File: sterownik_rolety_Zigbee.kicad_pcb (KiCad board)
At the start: 2 copper layers, 39 parts, among them J1 282836-5, J2 1725669, J3 53398-0567, Q1 BT136-600, Q2 BT136-600, Q3 MOC3032M, Q4 MOC3032M, U1 LTV-817, U2 LTV-817, U3 IRM-01-3.3, Y1 TXC 7R-32.000MEEV-T

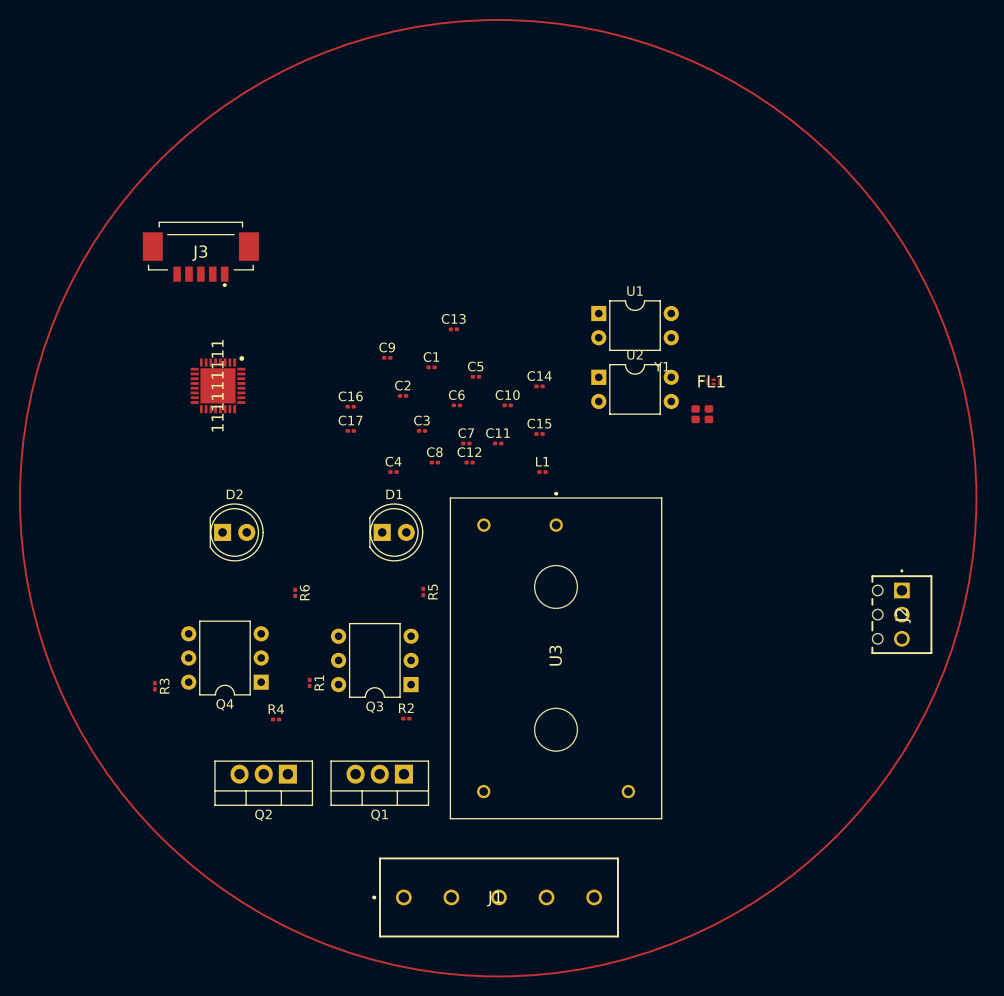
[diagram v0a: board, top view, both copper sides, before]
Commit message: kryształ kondensatory i interfejs podłączone z mikrokontrolerem
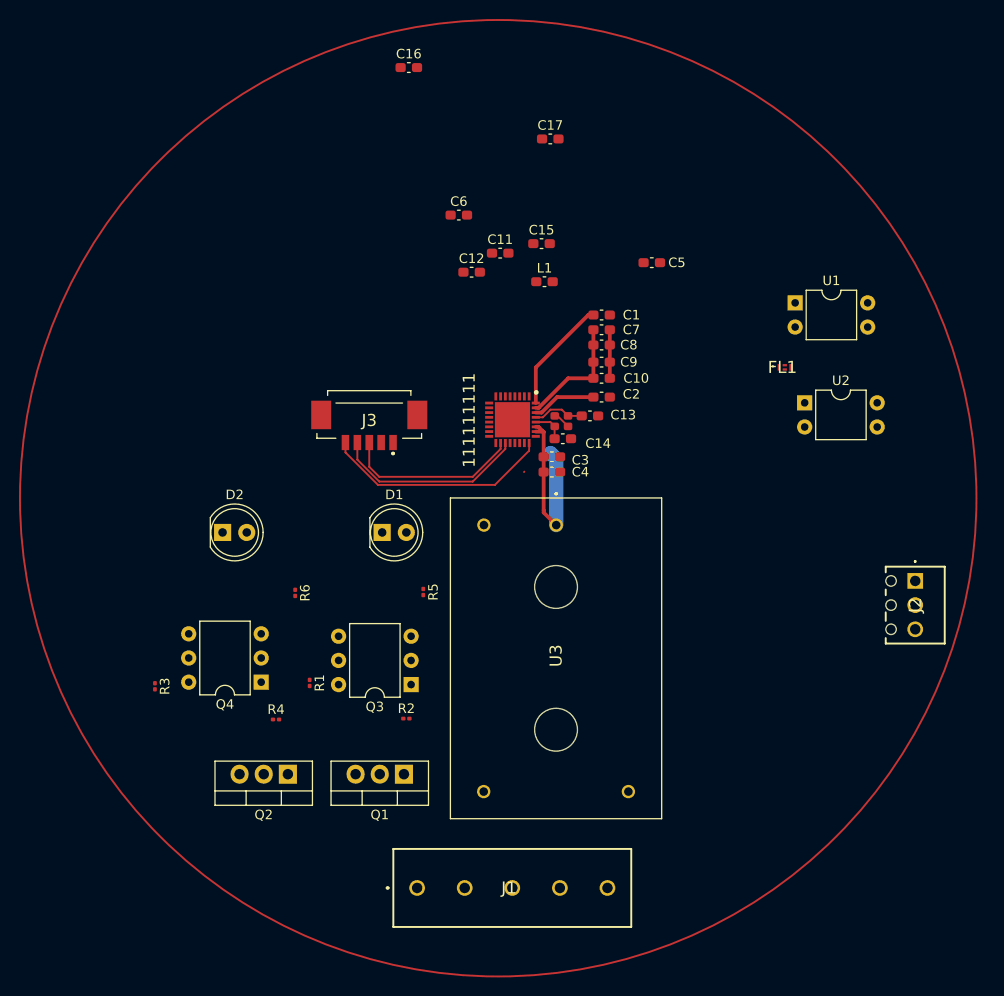
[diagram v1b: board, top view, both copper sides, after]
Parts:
- C1, C10, C11, C12, C13, C14, C15, C16, C17, C2, C3, C4, C5, C6, C7, C8, C9: footprint Capacitor_SMD:C_0201_0603Metric -> Capacitor_SMD:C_0603_1608Metric_Pad1.08x0.95mm_HandSolder
- L1: footprint Inductor_SMD:L_0201_0603Metric -> Capacitor_SMD:C_0603_1608Metric_Pad1.08x0.95mm_HandSolder
- moved C17 37.2 mm to (132.5, 60.0)
- moved C16 36.2 mm to (117.6, 52.5)
- moved 111111111 31.1 mm to (128.5, 89.5)
- moved J3 25.0 mm to (113.5, 89.6)
- moved C9 22.5 mm to (137.9, 83.5)
- moved C5 22.0 mm to (143.1, 73.0)
- moved U2 21.8 mm to (159.2, 87.7)
- moved C8 21.4 mm to (137.9, 81.7)
- moved C2 20.9 mm to (137.9, 87.1)
- moved U1 20.7 mm to (158.2, 77.2)
- moved C11 20.0 mm to (127.2, 72.0)
- moved C12 20.0 mm to (124.2, 74.0)
- moved C15 20.0 mm to (131.6, 71.0)
- moved C6 20.0 mm to (122.9, 68.0)
- moved L1 20.0 mm to (131.9, 75.0)
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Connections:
- C13 pad 1: GND -> Net-(111111111-OSC_IN)
- C13 pad 2: Net-(111111111-OSC_IN) -> GND
- C14 pad 1: GND -> Net-(111111111-OSC_OUT)
- C14 pad 2: Net-(111111111-OSC_OUT) -> GND
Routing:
- net VDD: track 0.00 -> 51.5 mm
- net Negated Reset: track 0.00 -> 24.0 mm
- net JTMS/SWDIO: track 0.00 -> 20.3 mm
- net JTCK/SWCLK: track 0.00 -> 18.6 mm
- net GND: track 0.00 -> 6.96 mm
- net Net-(111111111-OSC_IN): track 0.00 -> 5.43 mm
- net Net-(111111111-OSC_OUT): track 0.00 -> 3.48 mm

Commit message: połączenie ścieżkami, wylanie masy
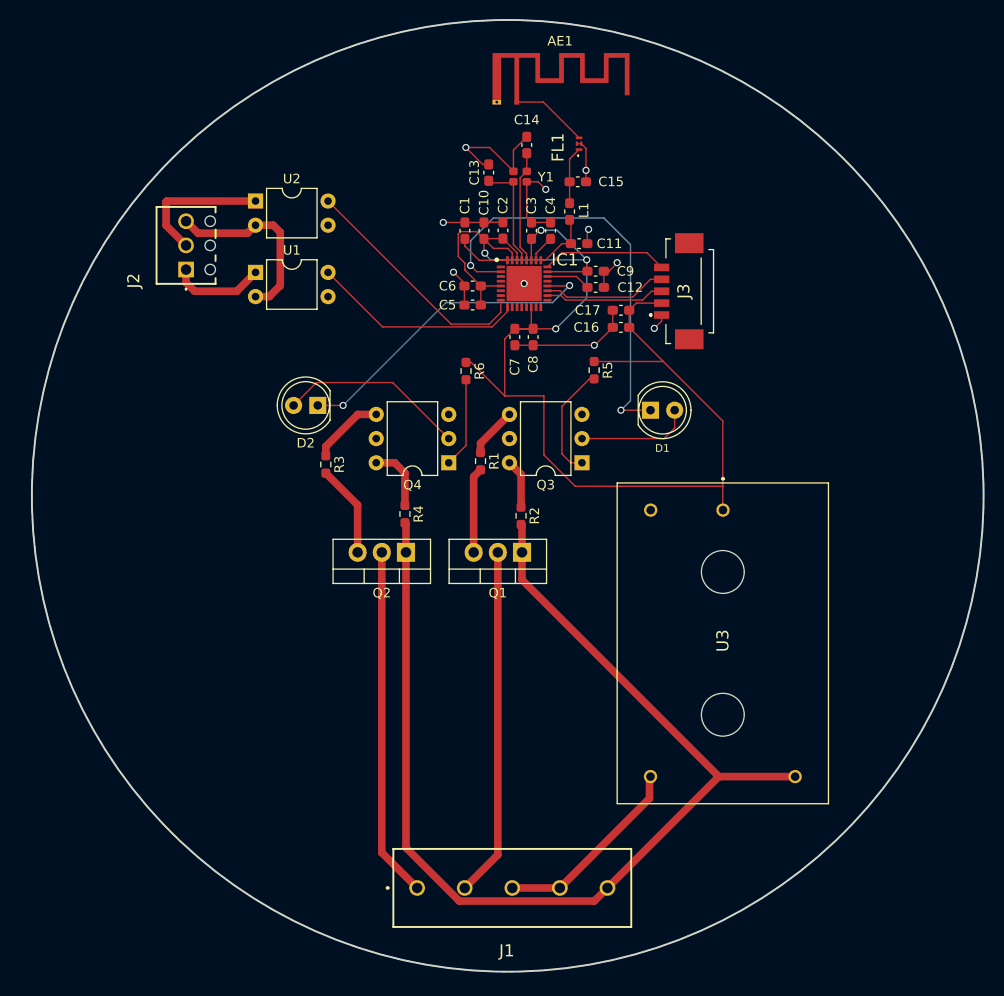
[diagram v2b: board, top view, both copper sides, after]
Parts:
- added AE1: Antenna, RF_Antenna:Texas_SWRA117D_2.4GHz_Right, F.Cu at (128.9, 56.1)
- L1: footprint Capacitor_SMD:C_0603_1608Metric_Pad1.08x0.95mm_HandSolder -> Inductor_SMD:L_0603_1608Metric_Pad1.05x0.95mm_HandSolder
- R1, R2, R3, R4, R5, R6: footprint Resistor_SMD:R_0201_0603Metric -> Resistor_SMD:R_0603_1608Metric_Pad0.98x0.95mm_HandSolder
- moved J2 83.3 mm to (94.2, 73.7), turned to 90 degrees
- moved U2 61.5 mm to (101.5, 66.5)
- moved U1 56.8 mm to (101.5, 74.0)
- moved J3 35.7 mm to (146.5, 76.0), turned to -90 degrees
- moved C16 35.2 mm to (139.9, 79.8), turned to 180 degrees
- moved FL1 31.9 mm to (135.5, 60.5), turned to 90 degrees
- moved C14 31.1 mm to (130.0, 60.6), turned to -90 degrees
- moved D1 31.0 mm to (143.0, 88.5)
- moved Q4 30.3 mm to (121.8, 94.0)
- moved R5 29.4 mm to (137.1, 84.3)
- moved Q3 29.4 mm to (135.8, 94.0)
- moved R1 29.4 mm to (125.1, 93.9)
- moved R3 29.4 mm to (108.9, 94.2)
- moved R6 29.4 mm to (123.6, 84.4)
- moved C13 27.7 mm to (126.0, 63.5), turned to -90 degrees
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- renumbered 111111111 to IC1
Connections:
- C1 pad 1: VDD -> Net-(IC1-VCAP)
- C13 pad 1: Net-(111111111-OSC_IN) -> GND
- C13 pad 2: GND -> Net-(IC1-OSC_IN)
- C14 pad 1: Net-(111111111-OSC_OUT) -> GND
- C14 pad 2: GND -> Net-(IC1-OSC_OUT)
- C4 pad 1: VDD -> Net-(IC1-VDDHPA)
- IC1 pad 26: VDD -> Net-(IC1-VDDHPA)
- IC1 pad 28: Net-(111111111-OSC_OUT) -> Net-(IC1-OSC_OUT)
- IC1 pad 29: Net-(111111111-OSC_IN) -> Net-(IC1-OSC_IN)
- IC1 pad 32: VDD -> Net-(IC1-VCAP)
- Y1 pad 1: Net-(111111111-OSC_OUT) -> Net-(IC1-OSC_OUT)
- Y1 pad 3: Net-(111111111-OSC_IN) -> Net-(IC1-OSC_IN)
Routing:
- net L_connector: track 0.00 -> 117.9 mm
- net VDD: track 51.5 -> 148.3 mm, vias 0 -> 4
- net GND: track 6.96 -> 56.7 mm, vias 0 -> 10
- net Motor_output_1: track 0.00 -> 45.9 mm, vias 0 -> 2
- net Q2_connector: track 0.00 -> 36.8 mm
- net Q1_connector: track 0.00 -> 36.7 mm
- net Motor_output_2: track 0.00 -> 34.0 mm, vias 0 -> 2
- net Net-(IC1-PA1): track 0.00 -> 25.3 mm
- net Net-(IC1-PA0): track 0.00 -> 22.4 mm
- net N_connector: track 0.00 -> 20.6 mm
- net Switch_Common: track 0.00 -> 19.8 mm
- net Net-(D2-A): track 0.00 -> 19.7 mm
- net Switch_Input_2: track 0.00 -> 14.9 mm
- net Net-(D1-A): track 0.00 -> 12.1 mm
- net Net-(Q3-Pad1): track 0.00 -> 12.1 mm
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- added copper zone on B.Cu, net GND
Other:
- board outline added: 100 x 100 mm

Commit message: poprawka wymiaru płytki
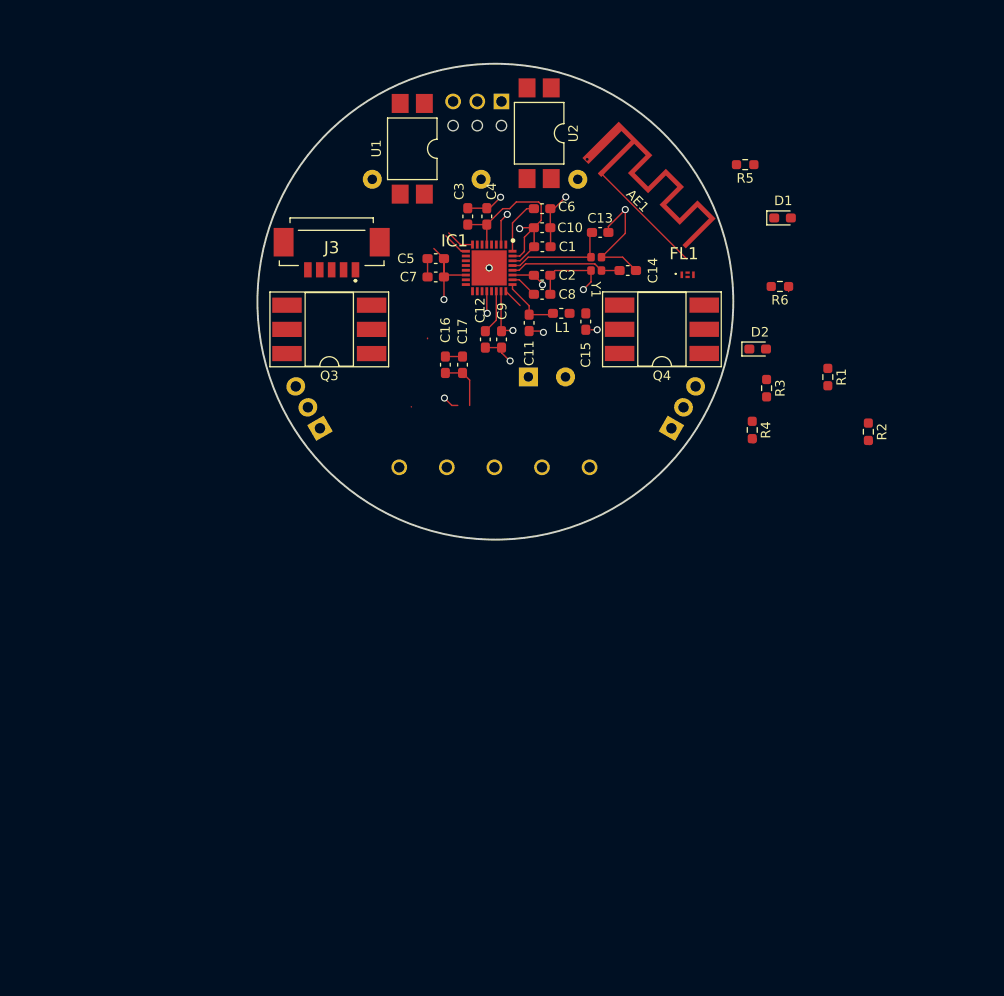
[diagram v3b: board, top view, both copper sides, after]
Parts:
- removed U3: IRM-01-3.3, Sterownik_roletyLibrary:IRM015
- added PS1: RAC05-3.3SK, Converter_ACDC:Converter_ACDC_RECOM_RAC05-xxSK_THT, B.Cu at (130.2, 85.0)
- D1, D2: value LD271 -> LED_Red; footprint LED_THT:LED_D5.0mm_IRGrey -> LED_SMD:LED_0603_1608Metric_Pad1.05x0.95mm_HandSolder
- J1, J2, Q1, Q2: moved to B.Cu
- Q3: value MOC3032M -> MOC3032MSR2M; footprint Package_DIP:DIP-6_W7.62mm -> Package_DIP:DIP-6_W8.89mm_SMDSocket_LongPads
- Q4: value MOC3032M -> MOC3032SR2M; footprint Package_DIP:DIP-6_W7.62mm -> Package_DIP:DIP-6_W8.89mm_SMDSocket_LongPads
- U1, U2: footprint Package_DIP:DIP-4_W7.62mm -> Package_DIP:SMDIP-4_W9.53mm
- moved J1 47.8 mm to (136.6, 94.5), turned to 180 degrees
- moved R3 47.0 mm to (155.2, 86.2)
- moved D2 46.6 mm to (154.3, 82.1), turned to 0 degrees
- moved J2 37.6 mm to (127.3, 56.1), turned to 180 degrees
- moved R4 37.5 mm to (153.7, 90.6)
- moved R1 37.5 mm to (161.6, 85.0)
- moved R2 37.5 mm to (165.9, 90.8)
- moved J3 36.9 mm to (109.9, 71.5), turned to 0 degrees
- moved R6 34.2 mm to (156.6, 75.5), turned to 180 degrees
- moved U2 30.6 mm to (131.3, 59.4), turned to -90 degrees
- moved Q3 30.0 mm to (109.2, 80.0)
- moved R5 26.8 mm to (152.9, 62.7), turned to 180 degrees
- moved Q4 26.4 mm to (144.2, 80.0)
- moved D1 24.5 mm to (156.9, 68.3)
- moved Q1 21.5 mm to (143.1, 86.7), turned to 0 degrees
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- renumbered C2 to C1, C3 to C2, C5 to C3, C6 to C4, C7 to C5, C1 to C6, C8 to C7, C4 to C8
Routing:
- net L_connector: track 117.9 -> 0.29 mm
- net VDD: track 148.3 -> 50.2 mm
- net Motor_output_1: track 45.9 -> 3.44 mm, vias 2 -> 1
- net Q2_connector: track 36.8 -> 0.00 mm
- net Q1_connector: track 36.7 -> 0.00 mm
- net Motor_output_2: track 34.0 -> 2.35 mm, vias 2 -> 1
- net Net-(IC1-PA1): track 25.3 -> 3.01 mm
- net N_connector: track 20.6 -> 0.00 mm
- net Switch_Common: track 19.8 -> 0.00 mm
- net Net-(D2-A): track 19.7 -> 0.00 mm
- net Net-(IC1-PA0): track 22.4 -> 2.77 mm
- net Switch_Input_2: track 14.9 -> 0.00 mm
- net GND: track 56.7 -> 42.8 mm, vias 10 -> 8
- net JTMS/SWDIO: track 13.1 -> 0.00 mm
- net JTCK/SWCLK: track 12.6 -> 0.00 mm
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- removed copper zone on B.Cu, net GND
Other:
- board size 100 x 100 mm -> 50 x 50 mm

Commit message: Wersja finalna
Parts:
- D1, D2: moved to B.Cu
- moved R2 54.3 mm to (111.8, 85.9)
- moved R1 52.2 mm to (109.4, 85.9)
- moved D1 49.5 mm to (108.9, 80.2), turned to 180 degrees
- moved R5 39.4 mm to (117.8, 80.6), turned to 90 degrees
- moved Q2 37.9 mm to (143.2, 86.5)
- moved Q1 37.2 mm to (105.9, 87.1)
- moved R6 22.2 mm to (137.5, 86.8), turned to 0 degrees
- moved R4 13.8 mm to (140.4, 87.0)
- moved R3 11.8 mm to (143.4, 87.0)
- moved D2 10.5 mm to (144.0, 80.0)
- moved C14 0.27 mm to (140.5, 73.6)
- moved Q3 0.15 mm to (109.2, 79.9), turned to 0 degrees
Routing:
- net VDD: track 50.2 -> 139.6 mm, vias 4 -> 6
- net L_connector: track 0.29 -> 69.4 mm
- net Negated Reset: track 2.12 -> 39.6 mm
- net Q1_connector: track 0.00 -> 28.0 mm
- net JTMS/SWDIO: track 0.00 -> 20.5 mm
- net Motor_output_1: track 3.44 -> 23.3 mm
- net Net-(Q4-Pad1): track 0.00 -> 19.4 mm
- net Motor_output_2: track 2.35 -> 21.1 mm
- net JTCK/SWCLK: track 0.00 -> 18.1 mm
- net N_connector: track 0.00 -> 17.6 mm
- net Switch_Input_2: track 0.00 -> 16.8 mm
- net Net-(Q3-Pad1): track 0.00 -> 16.1 mm
- net Switch_Common: track 0.00 -> 15.4 mm
- net Net-(FL1-IN): track 0.00 -> 13.6 mm
- net Net-(Q4-Pad4): track 0.00 -> 13.0 mm
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- added copper zone on B.Cu, net GND
